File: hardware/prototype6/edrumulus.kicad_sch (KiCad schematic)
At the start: 108 parts, among them J1 Trigger Connector, J2 Raspberry Pi GPIO pins, U1 ESP32-WROOM-32U, U2 AMS1117-3.3, U3 MCP1754S-3302xMB

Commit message: some more work on prototpye 6
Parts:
- removed C10, C9: 22µ, Capacitor_SMD:C_1210_3225Metric_Pad1.33x2.70mm_HandSolder, symbol Device:C
- removed C12, C13, C14, C15, C16, C17, C18, C19, C20, C21, C22, C23, C24, C25: 2n2, Capacitor_SMD:C_0603_1608Metric_Pad1.08x0.95mm_HandSolder, symbol Device:C
- removed C27: 22µ, Capacitor_SMD:C_0603_1608Metric_Pad1.08x0.95mm_HandSolder, symbol Device:C
- removed C28: 1µ, Capacitor_SMD:C_0603_1608Metric_Pad1.08x0.95mm_HandSolder, symbol Device:C
- removed C29, C3, C4, C5, C6, C7: 100n, Capacitor_SMD:C_0603_1608Metric_Pad1.08x0.95mm_HandSolder, symbol Device:C
- removed C30: 10n, Capacitor_SMD:C_0603_1608Metric_Pad1.08x0.95mm_HandSolder, symbol Device:C
- removed D1, D10, D11, D12, D13, D14, D15, D2, D3, D4, D5, D6, D7, D8, D9: BAV99, Package_TO_SOT_SMD:SOT-23, symbol Diode:BAV99
- removed D31: BOARD-LED, LED_SMD:LED_0603_1608Metric, symbol Device:LED
- removed FB2: FerriteBead, Inductor_SMD:L_1210_3225Metric_Pad1.42x2.65mm_HandSolder, symbol Device:FerriteBead
- removed J2: Raspberry Pi GPIO pins, Connector_PinSocket_2.54mm:PinSocket_2x20_P2.54mm_Vertical, symbol Connector_Generic:Conn_02x20_Odd_Even
- removed R12, R3, R4, R5, R6, R7, R8, R9: 100k, Resistor_SMD:R_0603_1608Metric_Pad0.98x0.95mm_HandSolder, symbol pspice:R
- removed R13, R14, R15, R16, R17, R18, R21, R22, R23, R24, R25, R26, R27: 22k, Resistor_SMD:R_0603_1608Metric_Pad0.98x0.95mm_HandSolder, symbol pspice:R
- removed R45, R46: 10k, Resistor_SMD:R_0603_1608Metric_Pad0.98x0.95mm_HandSolder, symbol pspice:R
- removed R47: 470, Resistor_SMD:R_0603_1608Metric_Pad0.98x0.95mm_HandSolder, symbol pspice:R
- removed U1: ESP32-WROOM-32U, RF_Module:ESP32-WROOM-32U, symbol RF_Module:ESP32-WROOM-32U
- removed U2: AMS1117-3.3, Package_TO_SOT_SMD:SOT-223-3_TabPin2, symbol Regulator_Linear:AMS1117-3.3
- added C? (x6): 2n2, Capacitor_SMD:C_0603_1608Metric_Pad1.08x0.95mm_HandSolder, symbol Device:C
- added D1, D10, D11, D19, D2, D20, D21, D22, D23, D24, D25, D26, D27, D28, D29, D30, D? (x12): BAT85, Diode_THT:D_DO-35_SOD27_P7.62mm_Horizontal, symbol Diode:BAT85
- added R? (x12): 22k, Resistor_SMD:R_1206_3216Metric_Pad1.30x1.75mm_HandSolder, symbol pspice:R
- added R? (x6): 100k, Resistor_SMD:R_1206_3216Metric_Pad1.30x1.75mm_HandSolder, symbol pspice:R
- added U1: ESP32-DEVKIT-V1, edrumulus:esp32_devkit_v1, symbol doit-esp32-devkit-v1:ESP32-DEVKIT-V1
- C1, C2: value 100n -> 2n2
- C11, C26, C31, C32, C33, C34, C35, C36, C37, C38, C8: footprint Capacitor_SMD:C_0603_1608Metric_Pad1.08x0.95mm_HandSolder -> (none)
- R1, R10, R11, R19, R2, R20, R29, R31, R35, R36: footprint Resistor_SMD:R_0603_1608Metric_Pad0.98x0.95mm_HandSolder -> Resistor_SMD:R_1206_3216Metric_Pad1.30x1.75mm_HandSolder
- R28: value 22k -> 10 kOhm; footprint Resistor_SMD:R_0603_1608Metric_Pad0.98x0.95mm_HandSolder -> Resistor_SMD:R_1206_3216Metric_Pad1.30x1.75mm_HandSolder
- R30, R32, R34, R38, R39, R40, R41, R42, R43, R44: value 22k -> 22 kOhm; footprint Resistor_SMD:R_0603_1608Metric_Pad0.98x0.95mm_HandSolder -> Resistor_SMD:R_1206_3216Metric_Pad1.30x1.75mm_HandSolder
- R33: value 10k -> 100k; footprint Resistor_SMD:R_0603_1608Metric_Pad0.98x0.95mm_HandSolder -> Resistor_SMD:R_1206_3216Metric_Pad1.30x1.75mm_HandSolder
- R37: value 10k -> 10 kOhm; footprint Resistor_SMD:R_0603_1608Metric_Pad0.98x0.95mm_HandSolder -> Resistor_SMD:R_1206_3216Metric_Pad1.30x1.75mm_HandSolder
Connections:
- net 3V3: now also R19.1, D10.1 (K), D11.1 (K), D23.1 (K), D24.1 (K), D25.1 (K), D26.1 (K), D29.1 (K), D30.1 (K), D?.1 (K), D?.1 (K), D?.1 (K), D?.1 (K), D?.1 (K), D?.1 (K), R?.1, R?.1, R?.1, R?.1, R?.1, R?.1; no longer C1.2, C2.2, R28.1
- net CRASH1-RING: now also R?.1; no longer R2.1
- net CRASH1-TIP: now also R?.1
- net GND: now also C1.2, C2.2, C?.2, C?.2, C?.2, C?.2, C?.2, C?.2, D1.2 (A), D19.2 (A), D2.2 (A), D20.2 (A), D21.2 (A), D22.2 (A), D27.2 (A), D28.2 (A), D?.2 (A), D?.2 (A), D?.2 (A), D?.2 (A), D?.2 (A), D?.2 (A), R?.2, R?.2, R?.2, R?.2, R?.2, R?.2, U1.14 (GND), U1.17 (GND); no longer C1.1, C2.1, R19.2
- net GPIO12: now also R29.1, R30.1, D20.1 (K), D24.2 (A), U1.12 (GPIO12_ADC2-CH5_HSPI-MISO_RTC-GPIO15); no longer R34.1
- net GPIO13: now also C?.1, D?.1 (K), D?.2 (A), R?.1, R?.2, R?.2, U1.13 (GPIO13_ADC2-CH4_HSPI-MOSI_RTC-GPIO14)
- net GPIO14: now also C?.1, D?.1 (K), D?.2 (A), R?.1, R?.2, R?.2, U1.11 (GPIO14_ADC2-CH6_HSPI-CLK_RTC-GPIO16); no longer R10.1, R20.2
- net GPIO15: now also R31.1, R32.1, D21.1 (K), D25.2 (A), U1.18 (GPIO15_ADC2-CH3_HSPI-CS0_RTC-GPIO13); no longer R29.1, R30.1
- net GPIO25: now also R28.1, U1.8 (GPIO25_ADC2-CH8_DAC1_RTC-GPIO6); no longer R35.2, R41.1, R43.2
- net GPIO26: now also C?.1, D?.1 (K), D?.2 (A), R?.1, R?.2, R?.2, U1.9 (GPIO26_ADC2-CH9_DAC2_RTC-GPIO7)
- net GPIO27: now also C?.1, D?.1 (K), D?.2 (A), R?.1, R?.2, R?.2, U1.10 (GPIO27_ADC2-CH7_RTC-GPIO17)
- net GPIO32: now also C?.1, D?.1 (K), D?.2 (A), R?.1, R?.2, R?.2, U1.6 (GPIO32_ADC1-CH4_RTC-GPIO9)
- net GPIO33: now also R33.1, R34.1, D22.1 (K), D26.2 (A), U1.7 (GPIO33_ADC1-CH5_RTC-GPIO8); no longer R31.1, R32.1
- net GPIO34: now also C?.1, D?.1 (K), D?.2 (A), R?.1, R?.2, R?.2, U1.4 (GPIO34_ADC1-CH6_RTC-GPIO4); no longer R11.1
- net GPIO35: now also C2.1, R10.1, R19.2, D1.1 (K), D10.2 (A), U1.5 (GPIO35_ADC1-CH7_RTC-GPIO5)
- net GPIO36: now also C1.1, R11.1, R20.2, D11.2 (A), D2.1 (K), U1.2 (GPIO36_ADC-CH0_SENS-VP_RTC-GPIO0)
- net GPIO39: now also D28.1 (K), D30.2 (A), U1.3 (GPIO39_ADC1-CH3_SENS-VN_RTC-GPIO3)
- net GPIO4: now also R35.2, R41.1, R43.2, D27.1 (K), D29.2 (A); no longer R33.1
- net HI-HAT-CONTROL-TIP: now also R28.2, D19.1 (K), D23.2 (A); no longer R33.2
- net HI-HAT-RING: now also R?.1
- net HI-HAT-TIP: now also R?.1; no longer R31.2
- net KICK-TIP: now also R33.2
- net RIDE-BELL-TIP: no longer R36.1
- net RIDE-RING: now also R?.1; no longer R35.1
- net RIDE-TIP: now also R?.1; no longer R1.1
- net SNARE-RING: now also R1.1
- net SNARE-TIP: now also R2.1
- net TOM1-RING: now also R35.1
- net TOM1-TIP: now also R36.1; no longer R29.2
- net TOM2-TIP: now also R29.2
- net TOM3-TIP: now also R31.2
- removed net GPIO2: R19.1, R28.2
- net RASPI-VIN renamed 5V
- net 5V: now also U1.15 (VIN)
- no-connect marks 42 -> 17
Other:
- note removed: "Bias Caps"
- note removed: "GPIO 25 and 26 are DAC pins which cause an incorrect DC offset estimation and DC offset drift which makes the spike cancellation algorithm work incorrectly."
- note removed: "Stitching Caps"
- moved on the sheet: C11, C26, C31, C32, C33, C34, C35, C36, C37, C38, C8, FB1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

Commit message: more work on prototype 6
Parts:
- removed D27, D28, D29, D30: BAT85, Diode_THT:D_DO-35_SOD27_P7.62mm_Horizontal, symbol Diode:BAT85
- removed R39, R40, R41, R42, R43, R44: 22 kOhm, Resistor_SMD:R_1206_3216Metric_Pad1.30x1.75mm_HandSolder, symbol pspice:R
- added C10, C12, C13, C14: 2n2, Capacitor_SMD:C_0603_1608Metric_Pad1.08x0.95mm_HandSolder, symbol Device:C
- added D17, D18: BAT85, Diode_THT:D_DO-35_SOD27_P7.62mm_Horizontal, symbol Diode:BAT85
- added R25, R27: 100k, Resistor_SMD:R_1206_3216Metric_Pad1.30x1.75mm_HandSolder, symbol pspice:R
- added R26: 22k, Resistor_SMD:R_1206_3216Metric_Pad1.30x1.75mm_HandSolder, symbol pspice:R
- R30, R34, R38: value 22 kOhm -> 22k
- R31, R33, R35, R36: value 100k -> 22k
- R32: value 22 kOhm -> 100k
- gave numbers to parts that had none: 36
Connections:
- net GPIO4 is gone; now on net GPIO39: R35.2
- net 3V3: now also D22.1 (K), R34.1, R35.1, R36.1
- net GND: now also R31.2, R33.2, C10.2, C12.2, C13.2, C14.2, D17.2 (A), D18.2 (A), R26.2; no longer D22.2 (A), R32.2, R34.2
- net GPIO12: now also C13.1
- net GPIO15: now also D22.2 (A), R34.2, C10.1, D17.1 (K), R25.1, R26.1; no longer D21.1 (K), D25.2 (A), R31.1, R32.1
- net GPIO33: now also D21.1 (K), R32.1, R36.2, C14.1; no longer D22.1 (K), R34.1
- net GPIO39: now also D25.2 (A), R31.1, C12.1, D18.1 (K), R27.1; no longer R36.2
- net KICK-TIP: now also R32.2; no longer R33.2
- net TOM1-RING: no longer R35.1
- net TOM1-TIP: now also R27.2; no longer R36.1
- net TOM3-TIP: now also R25.2; no longer R31.2
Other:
- title: Edrumulus Prototype 5 (ESP32) -> Edrumulus Prototype 6 (ESP32)
- moved on the sheet: C1, C11, C2, C26, C3, C31, C32, C33, C34, C35, C36, C37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

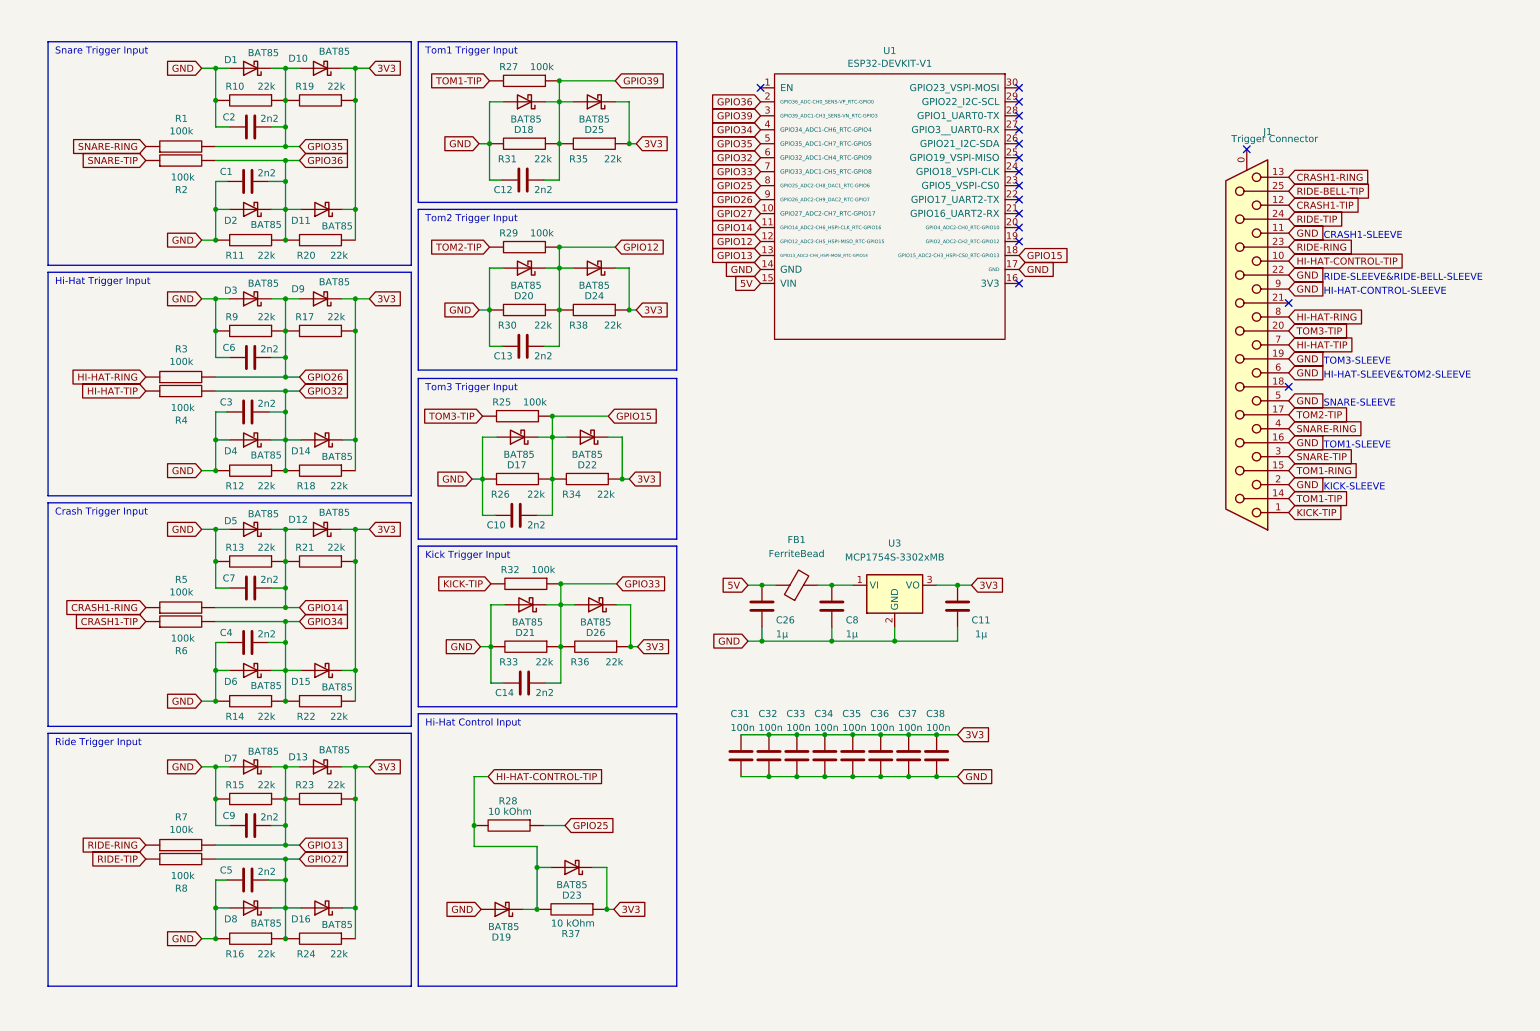
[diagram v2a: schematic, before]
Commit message: finished initial prototpye 6 schematics (still fine tuning has to be done)
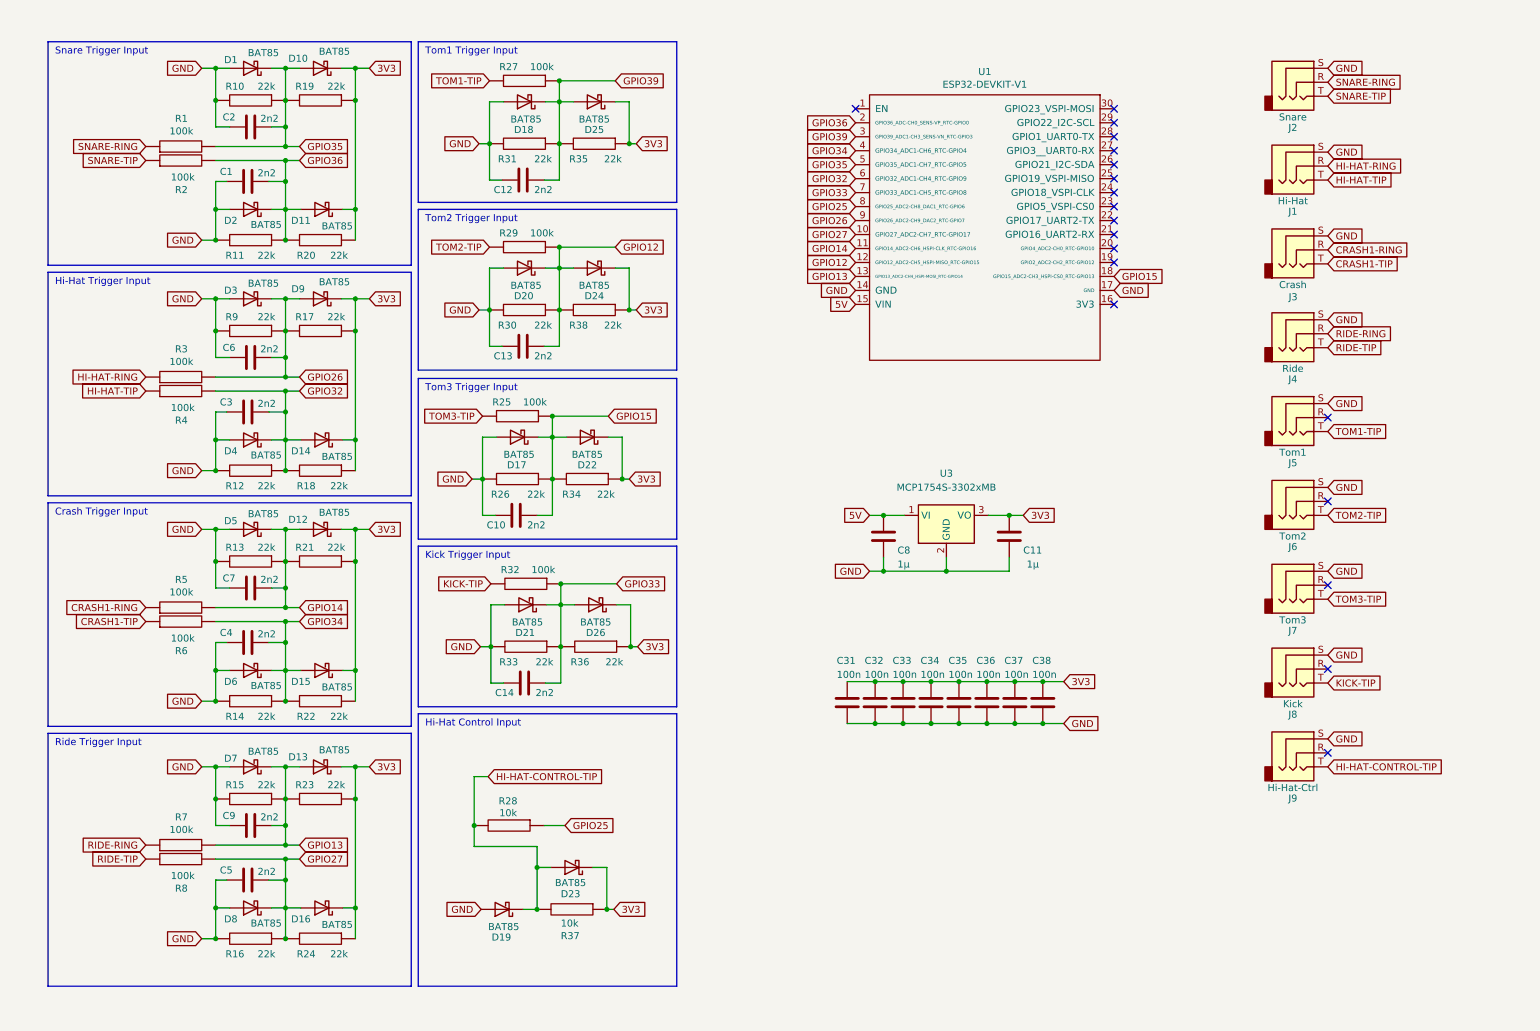
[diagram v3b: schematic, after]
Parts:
- removed C26: 1µ, symbol Device:C
- removed FB1: FerriteBead, Inductor_SMD:L_1210_3225Metric_Pad1.42x2.65mm_HandSolder, symbol Device:FerriteBead
- removed J1: Trigger Connector, Connector_Dsub:DSUB-25_Female_Horizontal_P2.77x2.84mm_EdgePinOffset7.70mm_Housed_MountingHolesOffset9.12mm, symbol Connector:DB25_Female_MountingHoles
- added J1: Hi-Hat, edrumulus:Jack_6.35mm_Neutrik_NMJ6HCD2_Horizontal, symbol Connector:AudioJack3
- added J2: Snare, edrumulus:Jack_6.35mm_Neutrik_NMJ6HCD2_Horizontal, symbol Connector:AudioJack3
- added J3: Crash, edrumulus:Jack_6.35mm_Neutrik_NMJ6HCD2_Horizontal, symbol Connector:AudioJack3
- added J4: Ride, edrumulus:Jack_6.35mm_Neutrik_NMJ6HCD2_Horizontal, symbol Connector:AudioJack3
- added J5: Tom1, edrumulus:Jack_6.35mm_Neutrik_NMJ6HCD2_Horizontal, symbol Connector:AudioJack3
- added J6: Tom2, edrumulus:Jack_6.35mm_Neutrik_NMJ6HCD2_Horizontal, symbol Connector:AudioJack3
- added J7: Tom3, edrumulus:Jack_6.35mm_Neutrik_NMJ6HCD2_Horizontal, symbol Connector:AudioJack3
- added J8: Kick, edrumulus:Jack_6.35mm_Neutrik_NMJ6HCD2_Horizontal, symbol Connector:AudioJack3
- added J9: Hi-Hat-Ctrl, edrumulus:Jack_6.35mm_Neutrik_NMJ6HCD2_Horizontal, symbol Connector:AudioJack3
- R1, R10, R11, R12, R13, R14, R15, R16, R17, R18, R19, R2, R20, R21, R22, R23, R24, R25, R26, R27, R29, R3, R30, R31, R32, R33, R34, R35, R36, R38, R4, R5, R6, R7, R8, R9: footprint Resistor_SMD:R_1206_3216Metric_Pad1.30x1.75mm_HandSolder -> (none)
- R28, R37: value 10 kOhm -> 10k; footprint Resistor_SMD:R_1206_3216Metric_Pad1.30x1.75mm_HandSolder -> (none)
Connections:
- net 5V: now also C8.1, U3.1 (VI)
- net CRASH1-RING: now also J3.R
- net CRASH1-TIP: now also J3.T
- net GND: now also J1.S, J2.S, J3.S, J4.S, J5.S, J6.S, J7.S, J8.S, J9.S
- net HI-HAT-CONTROL-TIP: now also J9.T
- net HI-HAT-RING: now also J1.R
- net HI-HAT-TIP: now also J1.T
- net KICK-TIP: now also J8.T
- net RIDE-RING: now also J4.R
- net RIDE-TIP: now also J4.T
- net SNARE-RING: now also J2.R
- net SNARE-TIP: now also J2.T
- net TOM1-TIP: now also J5.T
- net TOM2-TIP: now also J6.T
- net TOM3-TIP: now also J7.T
- no-connect marks 17 -> 19
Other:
- note removed: "CRASH1-SLEEVE"
- note removed: "HI-HAT-CONTROL-SLEEVE"
- note removed: "HI-HAT-SLEEVE&TOM2-SLEEVE"
- note removed: "KICK-SLEEVE"
- note removed: "RIDE-SLEEVE&RIDE-BELL-SLEEVE"
- note removed: "SNARE-SLEEVE"
- note removed: "TOM1-SLEEVE"
- note removed: "TOM3-SLEEVE"
- moved on the sheet: C11, C31, C32, C33, C34, C35, C36, C37, C38, C8, U1, U3
